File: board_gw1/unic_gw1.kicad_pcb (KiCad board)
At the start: 4 copper layers, 49.5 x 15.2 mm, 112 parts, among them Q1 2N7002, Q10 2N7002, Q11 2N7002, Q12 2N7002, Q13 2N7002, Q14 2N7002, Q15 2N7002, Q16 2N7002, Q17 2N7002, Q18 2N7002, Q19 2N7002, Q2 2N7002, Q20 2N7002, Q21 2N7002, Q22 2N7002, Q23 2N7002, Q24 2N7002, Q25 2N7002, Q26 2N7002, Q27 2N7002, Q28 2N7002, Q29 2N7002, Q3 2N7002, Q30 2N7002, Q31 2N7002, Q32 2N7002, Q33 2N7002, Q34 2N7002, Q35 2N7002, Q36 2N7002, Q37 2N7002, Q38 2N7002, Q39 2N7002, Q4 2N7002, Q40 2N7002, Q5 2N7002, Q6 2N7002, Q7 2N7002, Q8 2N7002, Q9 2N7002, U1 GW1N-LV9QN88C6_I5_, U2 LM3480-3.3, U3 AP2202K-ADJ, U4 APS6404L-3SQR-ZR, U6 AP62150Z6, U7 W25Q16JVUXIQ, X1 ASE-xxxMHz

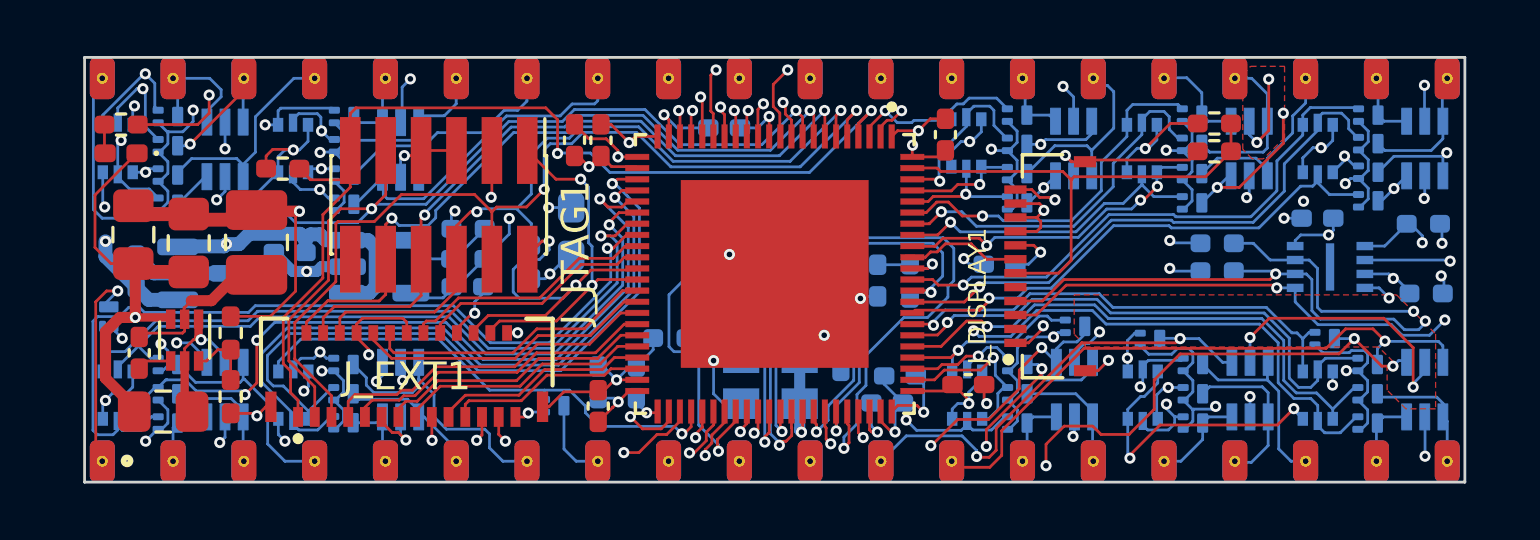
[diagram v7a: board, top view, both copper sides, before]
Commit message: Reworked switcher components and layout.
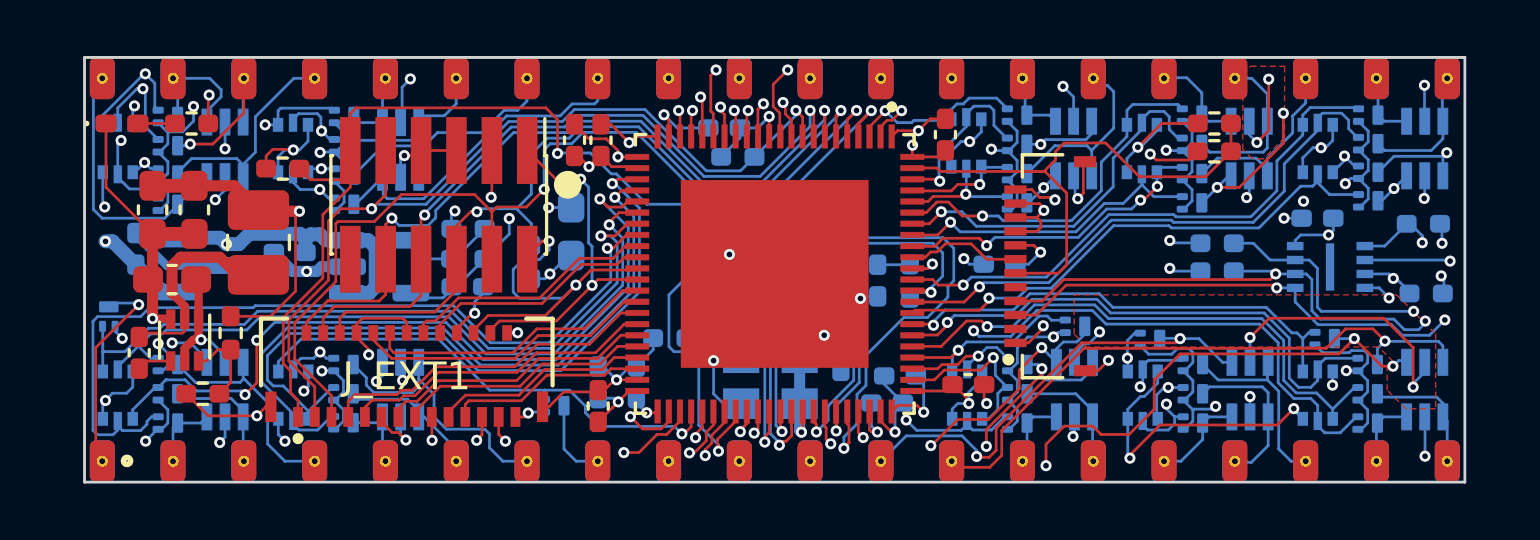
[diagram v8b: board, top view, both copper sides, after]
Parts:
- C1, C11, C13, C14, C15, C16, C17, C18, C19, C2, C20, C21, C22, C23, C4, C6, C9: value 0.1u -> 2.2u
- C5, C7, C8: footprint Capacitor_SMD:C_0805_2012Metric_Pad1.18x1.45mm_HandSolder -> Capacitor_SMD:C_0603_1608Metric_Pad1.08x0.95mm_HandSolder
- L1: value 3.3uH -> 10uH
- X1: value ASE-xxxMHz -> 27MHz
- moved R7 17.4 mm to (147.9, 91.2)
- moved C5 4.75 mm to (127.6, 95.6)
- moved R1 2.53 mm to (128.3, 90.0)
- moved C8 1.21 mm to (128.4, 93.1)
- moved C7 1.13 mm to (126.9, 93.1)
- moved LED_DONE1 1.07 mm to (125.8, 90.0), turned to 0 degrees
- moved R5 1.01 mm to (128.7, 99.7), turned to 180 degrees
- moved C2 0.81 mm to (126.3, 94.5)
- moved U2 0.28 mm to (128.7, 95.1)
- moved L1 0.07 mm to (130.7, 94.3)
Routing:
- net GND: track 85.3 -> 81.0 mm, vias 38 -> 39
- net Net-(U6-SW): track 4.61 -> 7.73 mm
- net /RECONFIG_N: track 34.7 -> 31.7 mm
- net /DONE: track 26.6 -> 24.3 mm
- net /LCD_RST_N: track 18.1 -> 20.4 mm
- net +3V3: track 75.2 -> 73.5 mm
- net /JTAG_TDO: track 24.8 -> 25.9 mm
- net /JTAG_TDI: track 24.9 -> 25.9 mm
- net /JTAG_SEL_N: track 36.6 -> 37.5 mm
- net /JTAG_TCK: track 25.3 -> 26.1 mm
- net /JTAG_TMS: track 33.6 -> 34.4 mm
- net Net-(U6-FB): track 2.41 -> 3.07 mm
- net /PIN1: track 11.5 -> 10.9 mm
- net +1V2: track 40.0 -> 40.6 mm
